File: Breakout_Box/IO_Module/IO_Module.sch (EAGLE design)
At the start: 5 parts, among them U1 AGND, U2 AGND, U3 AGND

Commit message: Licenses
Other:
- note added: "IO Module for Nexus Project by Cycfi Research is licensed under a Creative Commons Attribution-ShareAlike 4.0 International License. Copyright CYCFI Research Inc. 2013-2016"
- note removed: "Nu Project by Cycfi Research is licensed under a Creative Commons Attribution-ShareAlike 4.0 International License. Copyright CYCFI Research Inc. 2013-2016"
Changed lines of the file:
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@@
 <wire x1="233.45903125" y1="25.186403125" x2="233.45903125" y2="33.142509375" width="0" layer="94"/>
 <text x="252.73" y="6.985" size="2.54" layer="95">v0.9</text>
-<text x="12.7" y="7.62" size="2.54" layer="95">Nu Project by Cycfi Research is licensed under a Creative
-Commons Attribution-ShareAlike 4.0 International License.
+<text x="12.7" y="7.62" size="2.54" layer="95">IO Module for Nexus Project by Cycfi Research is licensed under a
+Creative Commons Attribution-ShareAlike 4.0 International License.
 Copyright CYCFI Research Inc. 2013-2016</text>
 <text x="200.025" y="11.43" size="2.54" layer="95">2016050</text>

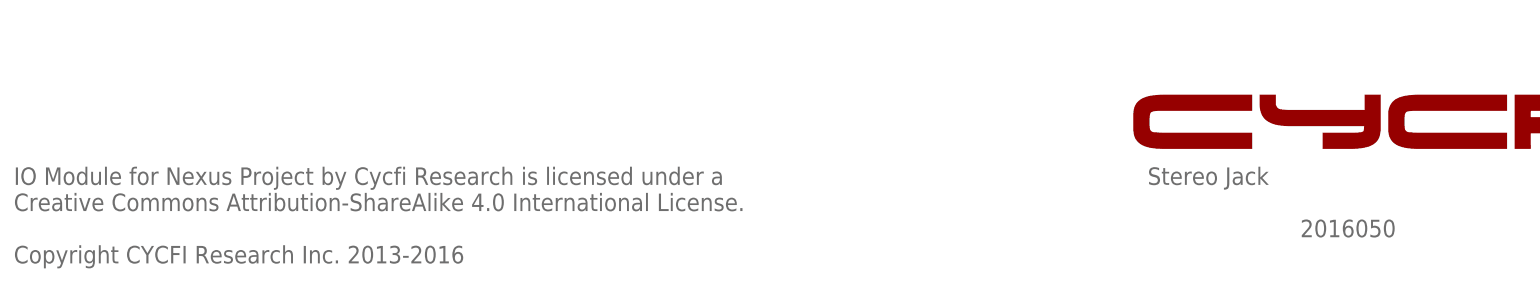
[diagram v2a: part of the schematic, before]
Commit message: Updated copyright and document number of schematics
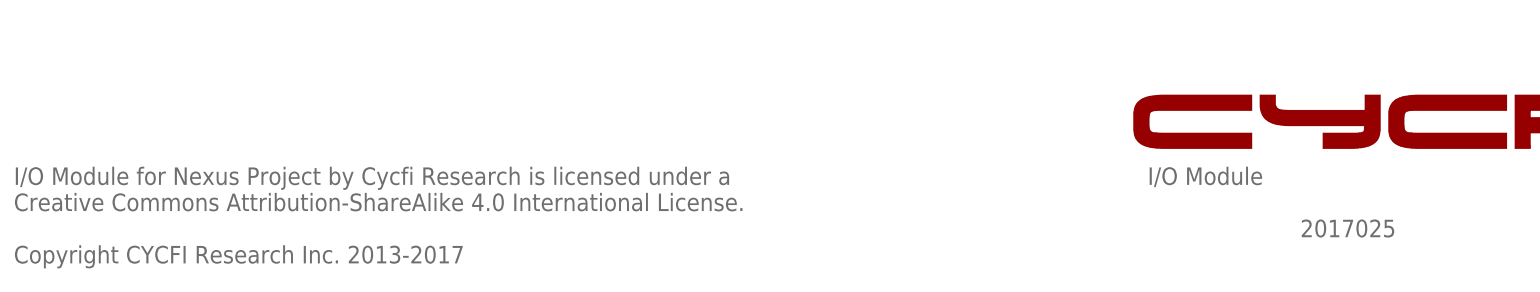
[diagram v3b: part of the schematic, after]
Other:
- note added: "2017025"
- note added: "I/O Module"
- note added: "I/O Module for Nexus Project by Cycfi Research is licensed under a Creative Commons Attribution-ShareAlike 4.0 International License. Copyright CYCFI Research Inc. 2013-2017"
- note removed: "2016050"
- note removed: "IO Module for Nexus Project by Cycfi Research is licensed under a Creative Commons Attribution-ShareAlike 4.0 International License. Copyright CYCFI Research Inc. 2013-2016"
- note removed: "Stereo Jack"
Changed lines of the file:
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@@
 <?xml version="1.0" encoding="utf-8"?>
 <!DOCTYPE eagle SYSTEM "eagle.dtd">
-<eagle version="6.3">
+<eagle version="7.6.0">
 <drawing>
 <settings>
@@
 <description>MAIN</description>
 <plain>
-<text x="177.8" y="19.05" size="2.54" layer="95">Stereo Jack</text>
+<text x="177.8" y="19.05" size="2.54" layer="95">I/O Module</text>
 <text x="252.73" y="6.985" size="2.54" layer="95">v0.9</text>
-<text x="12.7" y="7.62" size="2.54" layer="95">IO Module for Nexus Project by Cycfi Research is licensed under a
+<text x="12.7" y="7.62" size="2.54" layer="95">I/O Module for Nexus Project by Cycfi Research is licensed under a
 Creative Commons Attribution-ShareAlike 4.0 International License.
-Copyright CYCFI Research Inc. 2013-2016</text>
-<text x="200.025" y="11.43" size="2.54" layer="95">2016050</text>
+Copyright CYCFI Research Inc. 2013-2017</text>
+<text x="200.025" y="11.43" size="2.54" layer="95">2017025</text>
 <text x="66.04" y="121.92" size="1.778" layer="95">CH1</text>
 <text x="66.04" y="119.38" size="1.778" layer="95">CH2</text>

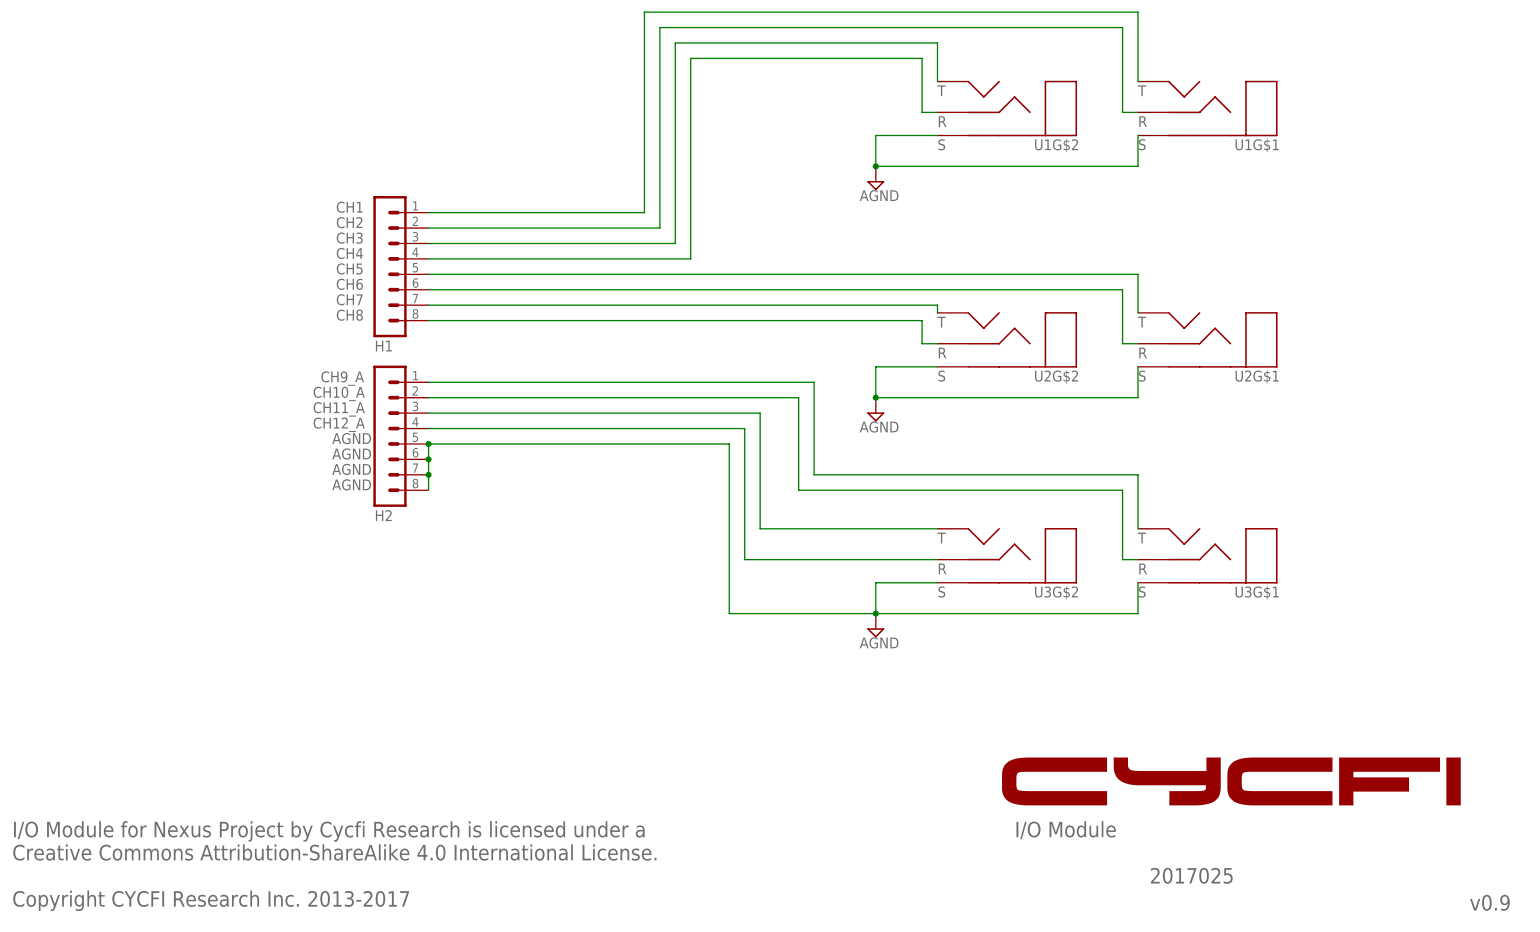
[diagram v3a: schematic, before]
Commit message: Update: Main Board MIDI Board MCU Board IO Board
Delete:
Mixer Board
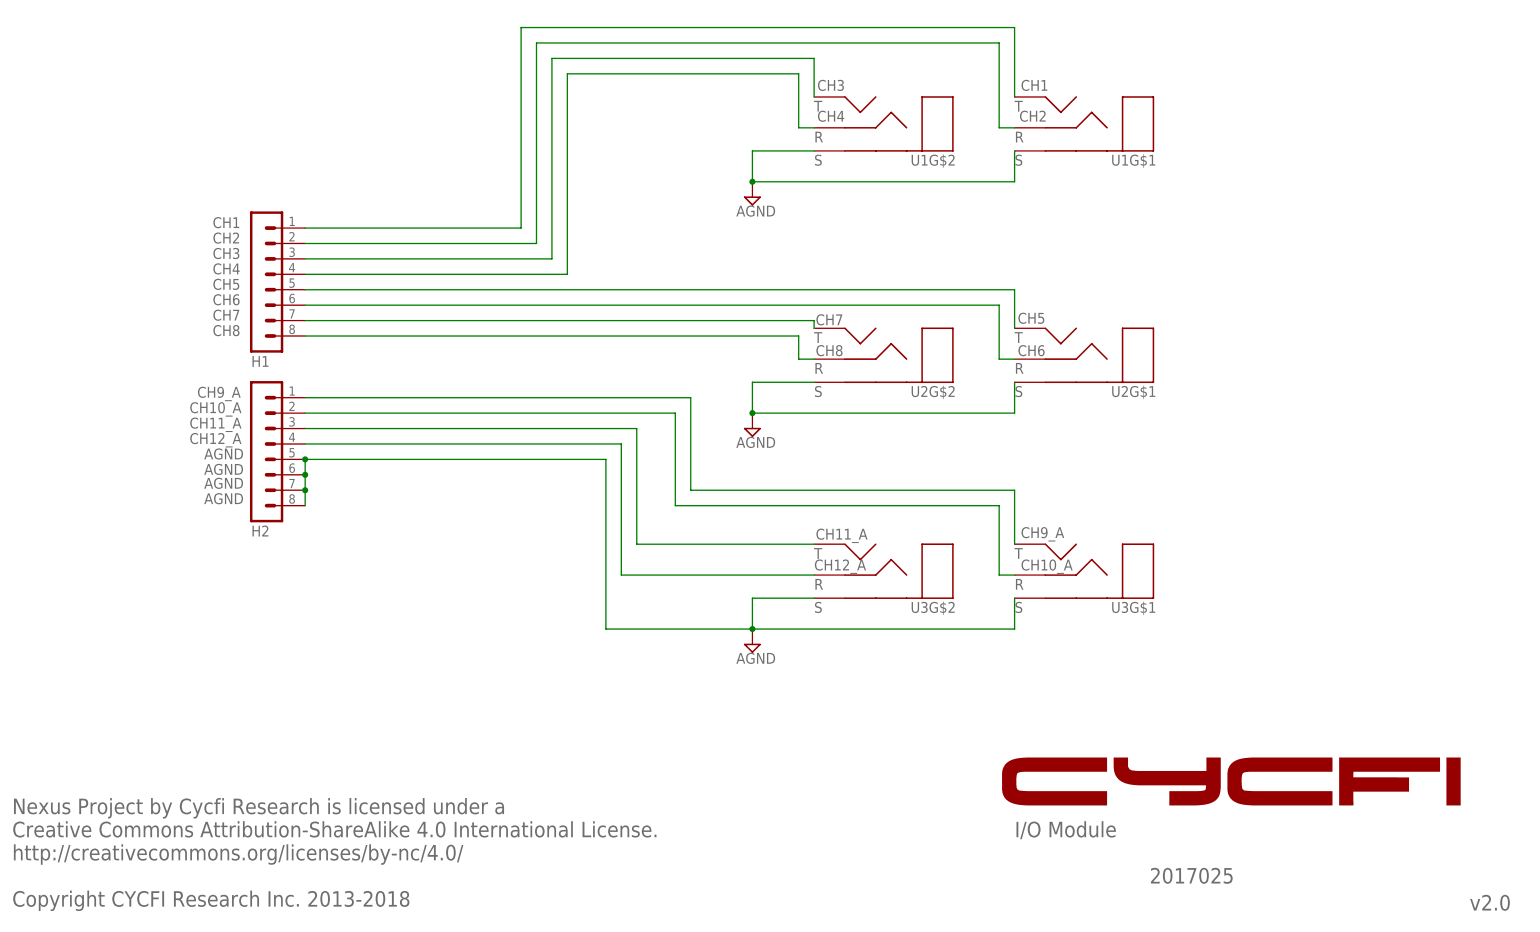
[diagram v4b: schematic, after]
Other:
- note added: "Nexus Project by Cycfi Research is licensed under a Creative Commons Attribution-ShareAlike 4.0 International License. http://creativecommons.org/licenses/by-nc/4.0/ Copyright CYCFI Research Inc. 2013-2018"
- note added: "v2.0"
- note removed: "I/O Module for Nexus Project by Cycfi Research is licensed under a Creative Commons Attribution-ShareAlike 4.0 International License. Copyright CYCFI Research Inc. 2013-2017"
- note removed: "v0.9"
- moved on the sheet: H1, H2, U1G$1, U1G$2, U2G$1, U2G$2, U3G$1, U3G$2
